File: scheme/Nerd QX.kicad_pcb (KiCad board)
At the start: 6 copper layers, 89 x 184 mm, 257 parts, among them J1 Connector 02x01, J2 Conn_01x04, M1 Fan_4pin, M2 Fan_4pin, M3 Fan_4pin, U10 CSD95472Q5MC, U19 BM1370_mode1, U2 TMUX1109RSVR, U20 BM1370_mode1, U25 BM1370_mode1, U26 BM1370_mode1, U3 TPS53647, U30 T-Display-S3, U32 EMC2302-1, U33 TXU0102-DCU, U35 TXU0304PW, U36 MCP1824T-1202E, U37 TMP1075, U38 TMP1075, U4 CSD95472Q5MC, U5 TMP451, U6 AP3211, U7 MCP1824T-0802E, U8 25MHz, U9 CSD95472Q5MC

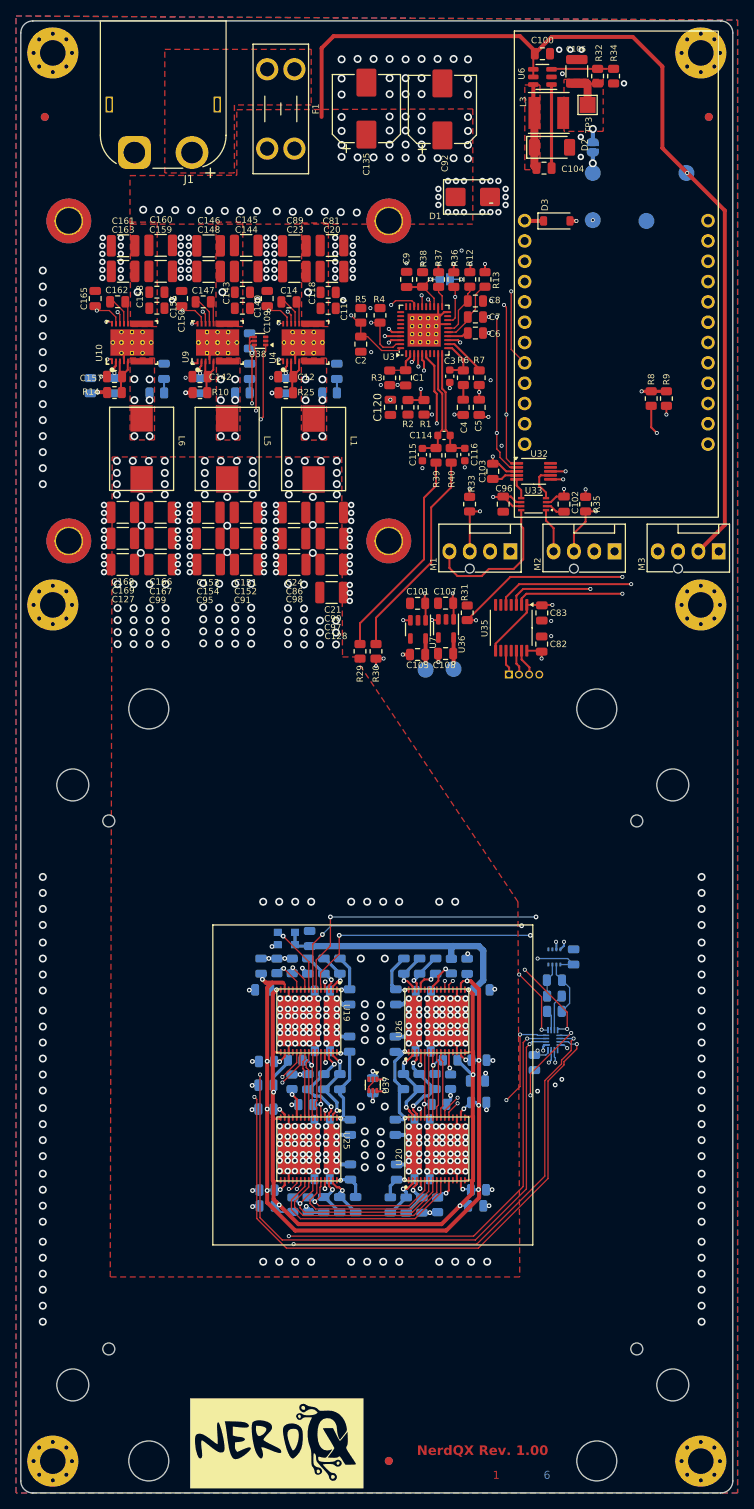
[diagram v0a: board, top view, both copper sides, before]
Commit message: silkscreen update for prototype boards
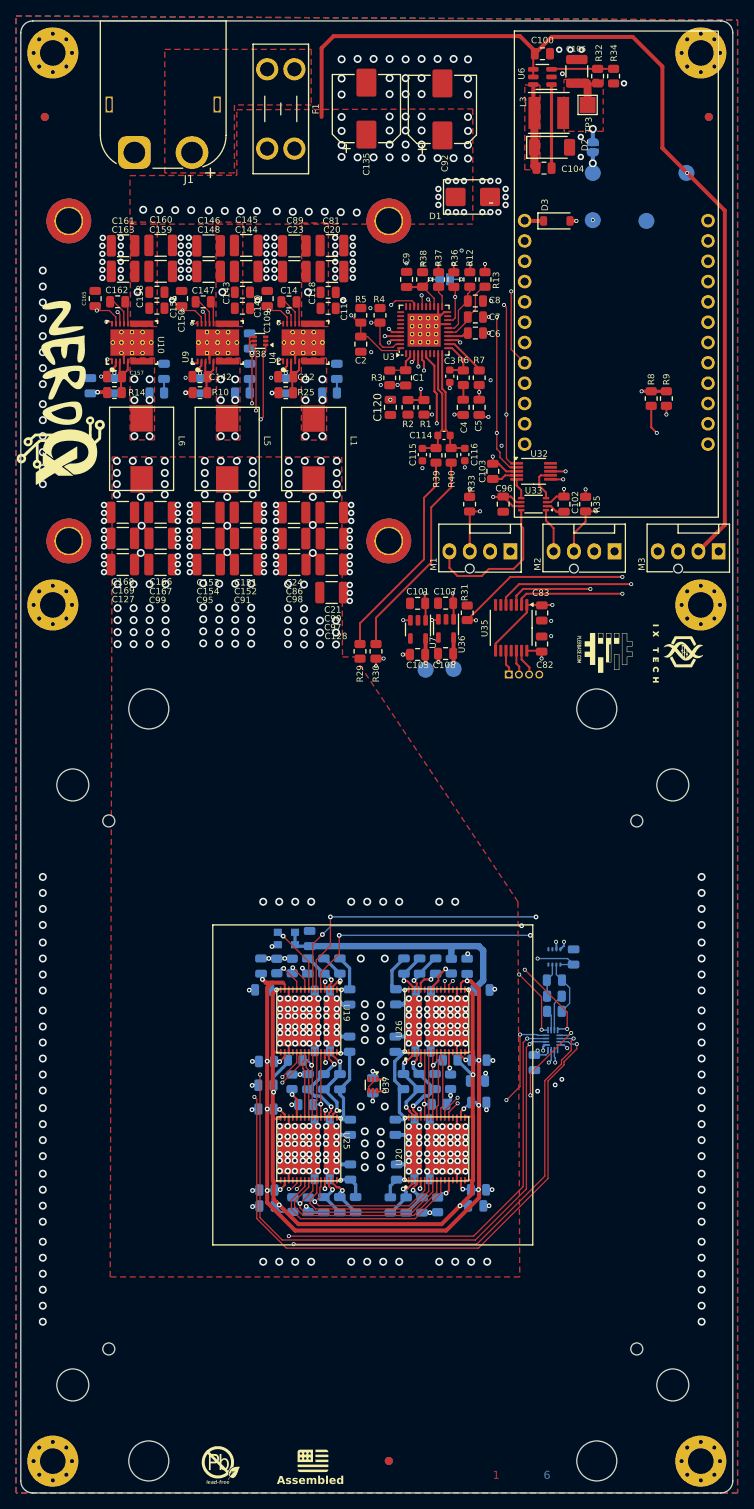
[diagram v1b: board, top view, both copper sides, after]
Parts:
- removed the G*** at (81.0, 190.8)
- added G***: LOGO, ix_imgs:flag, F.Cu at (85.5, 193.0)
- added G***: LOGO, ix_imgs:plebbase, F.Cu at (122.0, 92.0)
- added G***: LOGO, ix_imgs:ix_small, F.Cu at (131.0, 92.5)
- added G***: LOGO, kicad_foot:PBfree, F.Cu at (74.0, 193.5)
- added G***: LOGO, ix_imgs:QX, F.Cu at (54.0, 59.5)
- added G***: LOGO, ix_imgs:plebbase_big, B.Cu at (124.0, 61.5)
- added G***: LOGO, ix_imgs:ix_large, B.Cu at (123.3, 48.0)
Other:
- board text added: "Assembled"
- board text added: "Collaboration of: phil31 plebbase.com ixtech.xyz shufps"
- board text added: "rev1.0"
- board text removed: "NerdQX Rev. 1.00"
